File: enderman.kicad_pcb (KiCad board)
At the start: 2 copper layers, 29 x 98 mm, 22 parts, among them U1 4030, U2 LM556

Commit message: v2.0 RTM
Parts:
- added LS1: Speaker_Crystal, Library:Piezo PKMCS0909E4000-R1, B.Cu at (135.4, 68.2)
- BT1, BT2, BT3: footprint Library:BatteryHolder_Keystone_3030 -> Library:BatteryHolder_Keystone_2996
- C2, C5: value 1u -> 47n
- R2: value 4k7 -> R_Photo; footprint Resistor_SMD:R_0603_1608Metric -> Library:SMD2.4x3.6
- R3: value 5k1 -> R_Photo; footprint Resistor_SMD:R_0603_1608Metric -> Library:SMD2.4x3.6
- moved BT3 30.3 mm to (132.3, 52.8)
- moved BT2 29.9 mm to (139.5, 81.6)
- moved C1 25.4 mm to (145.8, 82.8)
- moved BT1 13.0 mm to (137.9, 82.8), turned to -90 degrees
- moved R5 5.19 mm to (133.4, 59.5), turned to -90 degrees
- moved R3 4.21 mm to (132.2, 89.0), turned to 90 degrees
- moved C6 3.65 mm to (133.4, 80.2), turned to 90 degrees
- moved R2 1.70 mm to (134.6, 74.0)
- moved C2 1.40 mm to (143.0, 72.2), turned to 90 degrees
- moved R1 1.02 mm to (138.2, 71.4)
- moved TP2 0.89 mm to (132.6, 42.0)
- moved TP1 0.89 mm to (144.8, 42.0)
- moved C4 0.60 mm to (139.0, 88.0)
- moved C3 0.59 mm to (140.2, 76.0), turned to 180 degrees
- moved R4 0.25 mm to (136.4, 87.2)
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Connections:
- U1 pad 1: Net-(U2B-Q) -> GND
- U1 pad 10: unconnected-(U1-Pad10) -> Net-(D2-K)
- U1 pad 11: unconnected-(U1-Pad11) -> Net-(LS1-Pad1)
- U1 pad 12: GND -> Net-(D1-K)
- U1 pad 13: GND -> +6V
- U1 pad 2: Net-(U2A-Q) -> GND
- U1 pad 3: Net-(D1-K) -> unconnected-(U1-Pad3)
- U1 pad 4: Net-(D2-K) -> Net-(D1-K)
- U1 pad 5: Net-(D1-K) -> Net-(U2A-Q)
- U1 pad 6: +6V -> Net-(U2B-Q)
- U1 pad 8: GND -> Net-(D1-K)
- U1 pad 9: GND -> +6V
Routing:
- net GND: track 68.7 -> 101.6 mm, vias 5 -> 12
- net +6V: track 84.6 -> 97.6 mm, vias 3 -> 2
- net Net-(D2-K): track 28.0 -> 17.2 mm, vias 2 -> 0
- net Net-(U2B-Q): track 14.2 -> 23.1 mm, vias 2 -> 0
- net Net-(BT1-+): track 39.9 -> 47.3 mm
- net Net-(D1-A): track 18.3 -> 12.2 mm
- net Net-(LS1-Pad1): track 0.00 -> 5.02 mm, vias 0 -> 1
- net Net-(U2A-THR): track 13.9 -> 17.3 mm
- net Net-(U2B-THR): track 17.4 -> 19.9 mm
- net Net-(U2A-Q): track 18.8 -> 16.5 mm
- net Net-(U2B-DIS): track 7.13 -> 8.81 mm
- net Net-(U2A-DIS): track 4.66 -> 6.24 mm
- net Net-(D1-K): track 27.5 -> 28.8 mm, vias 2 -> 0
- net Net-(U2B-CV): track 2.70 -> 4.00 mm
- net Net-(BT2--): track 45.3 -> 46.3 mm
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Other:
- board text added: "REYWAS INDSTRIES 2025"

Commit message: fix typo
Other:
- board text added: "REYWAS INDUSTRIES 2025"
- board text removed: "REYWAS INDSTRIES 2025"
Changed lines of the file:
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@@
   (gr_line (start 141.026138 93.039062) (end 141.026138 137.501956)
     (stroke (width 0.2) (type solid)) (layer "Edge.Cuts"))
-  (gr_text "REYWAS INDSTRIES 2025" (at 151.8 91.6 90) (layer "B.SilkS")
+  (gr_text "REYWAS INDUSTRIES 2025" (at 151.8 91.6 90) (layer "B.SilkS")
     (effects (font (size 1 1) (thickness 0.1)) (justify left bottom mirror))
   )

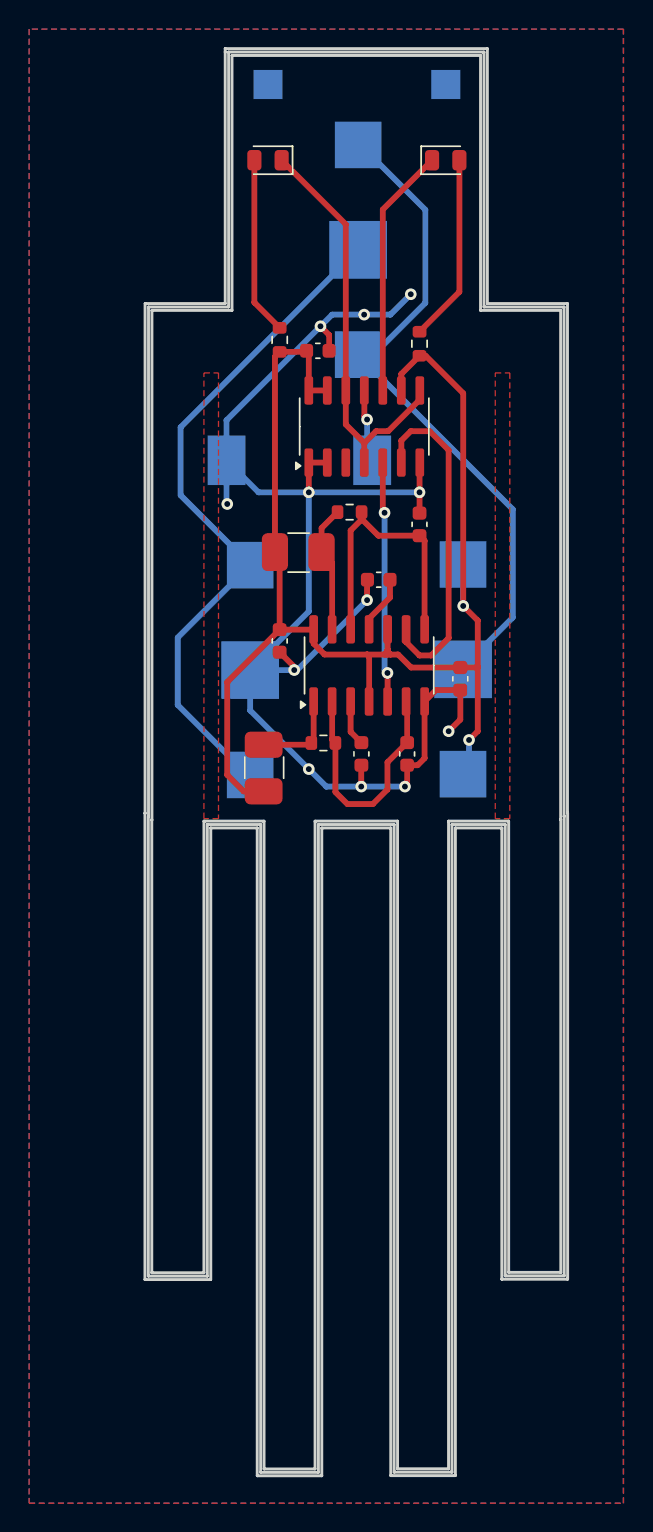
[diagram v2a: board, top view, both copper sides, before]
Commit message: add option for 2x drive to buzzer
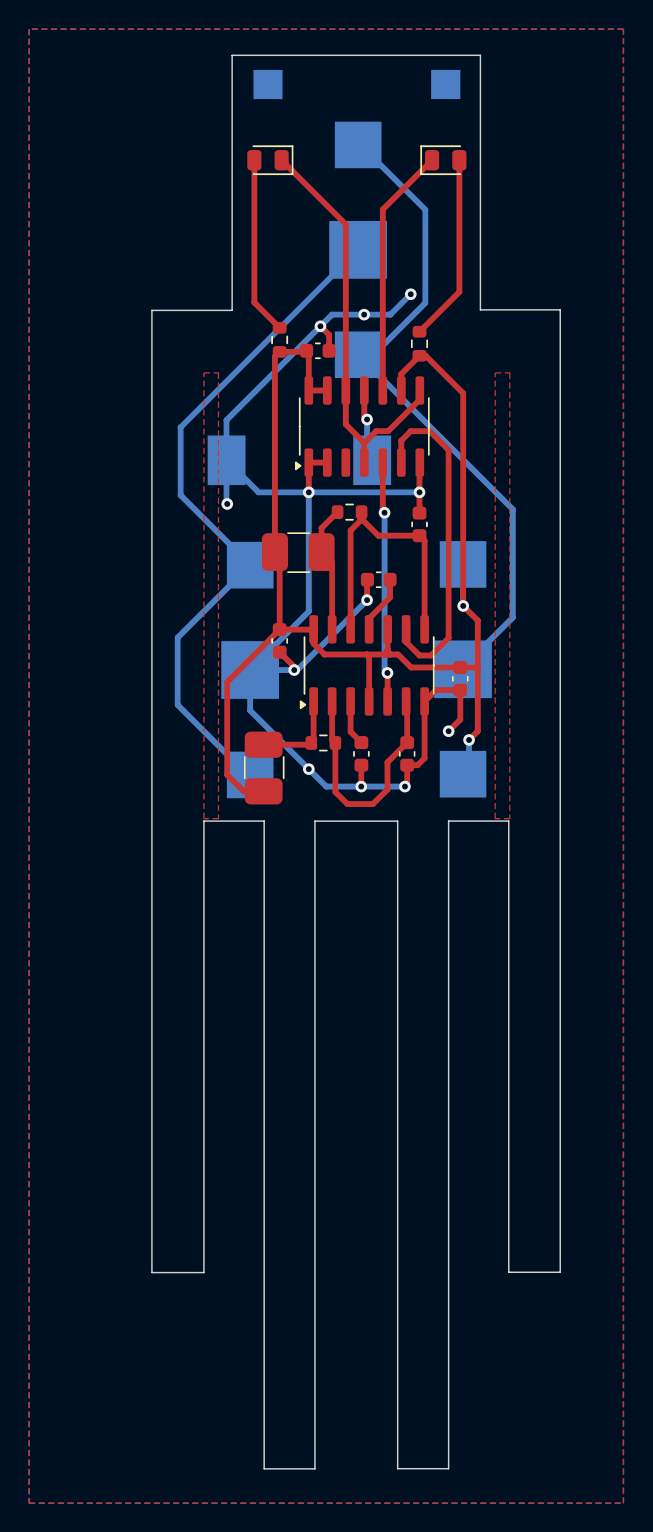
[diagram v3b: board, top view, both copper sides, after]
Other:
- board size 29 x 98 mm -> 28 x 97 mm

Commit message: xor routing
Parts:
- added JP1: SolderJumper_2_Open, Jumper:SolderJumper-2_P1.3mm_Open_RoundedPad1.0x1.5mm, B.Cu at (138.8, 74.2)
- added SW1: SW_SPDT, Button_Switch_SMD:SW_SPDT_PCM12, B.Cu at (127.7, 62.6)
- C1: value 1u -> 2u2
- moved R3 28.8 mm to (145.4, 63.4), turned to 180 degrees
- moved C1 26.7 mm to (129.8, 61.4), turned to 0 degrees
- moved C5 16.9 mm to (133.0, 73.8), turned to 180 degrees
- moved C2 16.4 mm to (131.6, 84.0), turned to 0 degrees
- moved C4 16.2 mm to (139.8, 71.8), turned to 0 degrees
- moved R1 16.1 mm to (134.6, 87.0), turned to 90 degrees
- moved R2 14.9 mm to (139.2, 88.2), turned to -90 degrees
- moved R4 13.9 mm to (139.8, 73.8), turned to 180 degrees
- moved C6 9.66 mm to (142.0, 84.6)
- moved C3 9.42 mm to (135.3, 84.0)
- moved R6 4.64 mm to (138.6, 61.3), turned to 0 degrees
- moved U2 4.33 mm to (136.5, 78.8), turned to -90 degrees
- moved LS1 4.05 mm to (139.5, 68.2)
- moved C7 3.01 mm to (133.2, 61.4), turned to 0 degrees
- moved U1 2.82 mm to (136.6, 66.6)
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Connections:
- BT2 pad 1: +6V -> Net-(BT2-+)
- BT2 pad 2: Net-(BT2--) -> Net-(BT1-+)
- BT3 pad 1: Net-(BT2--) -> Net-(BT3-+)
- BT3 pad 2: Net-(BT1-+) -> Net-(BT2-+)
- D1 pad 2: Net-(D1-A) -> +6V
- D2 pad 2: Net-(D2-A) -> +6V
- R5 pad 1: Net-(D1-A) -> Net-(R5-Pad1)
- R5 pad 2: +6V -> Net-(D1-K)
- R6 pad 1: Net-(D2-A) -> Net-(R6-Pad1)
- R6 pad 2: +6V -> Net-(D2-K)
- U1 pad 1: GND -> Net-(U2A-Q)
- U1 pad 10: Net-(D2-K) -> Net-(R6-Pad1)
- U1 pad 12: Net-(D1-K) -> Net-(R5-Pad1)
- U1 pad 2: GND -> Net-(U2B-Q)
- U1 pad 3: unconnected-(U1-Pad3) -> Net-(R5-Pad1)
- U1 pad 4: Net-(D1-K) -> Net-(JP1-A)
- U1 pad 5: Net-(U2A-Q) -> Net-(R5-Pad1)
- U1 pad 6: Net-(U2B-Q) -> +6V
- U1 pad 8: Net-(D1-K) -> Net-(R5-Pad1)
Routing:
- net GND: track 101.6 -> 0.00 mm, vias 12 -> 0
- net Net-(BT2--): track 46.3 -> 0.00 mm
- net Net-(BT2-+): track 0.00 -> 44.4 mm
- net Net-(BT3-+): track 0.00 -> 28.6 mm
- net +6V: track 97.6 -> 116.6 mm, vias 2 -> 1
- net Net-(R5-Pad1): track 0.00 -> 17.3 mm
- net Net-(D1-K): track 28.8 -> 13.5 mm
- net Net-(D2-A): track 12.9 -> 0.00 mm
- net Net-(D1-A): track 12.2 -> 0.00 mm
- net Net-(BT1-+): track 47.3 -> 37.8 mm
- net Net-(U2A-DIS): track 6.24 -> 14.5 mm
- net Net-(U2A-Q): track 16.5 -> 8.31 mm, vias 2 -> 0
- net Net-(JP1-A): track 0.00 -> 6.48 mm, vias 0 -> 1
- net Net-(U2B-DIS): track 8.81 -> 14.0 mm
- net Net-(JP1-B): track 5.02 -> 0.00 mm, vias 1 -> 0
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
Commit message: routed xor version with better placement of switch
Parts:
- moved C1 4.40 mm to (133.2, 58.6), turned to 180 degrees
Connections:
- SW1 pad 1: +6V -> unconnected-(SW1-A-Pad1)
- SW1 pad 3: unconnected-(SW1-C-Pad3) -> +6V
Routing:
- net GND: track 0.00 -> 65.2 mm, vias 0 -> 5
- net Net-(JP1-B): track 0.00 -> 18.0 mm, vias 0 -> 1
- net Net-(U2A-THR): track 13.6 -> 14.4 mm, vias 0 -> 2
